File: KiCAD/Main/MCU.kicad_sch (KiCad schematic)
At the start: 8 parts, among them U1 STM32H730VBTx

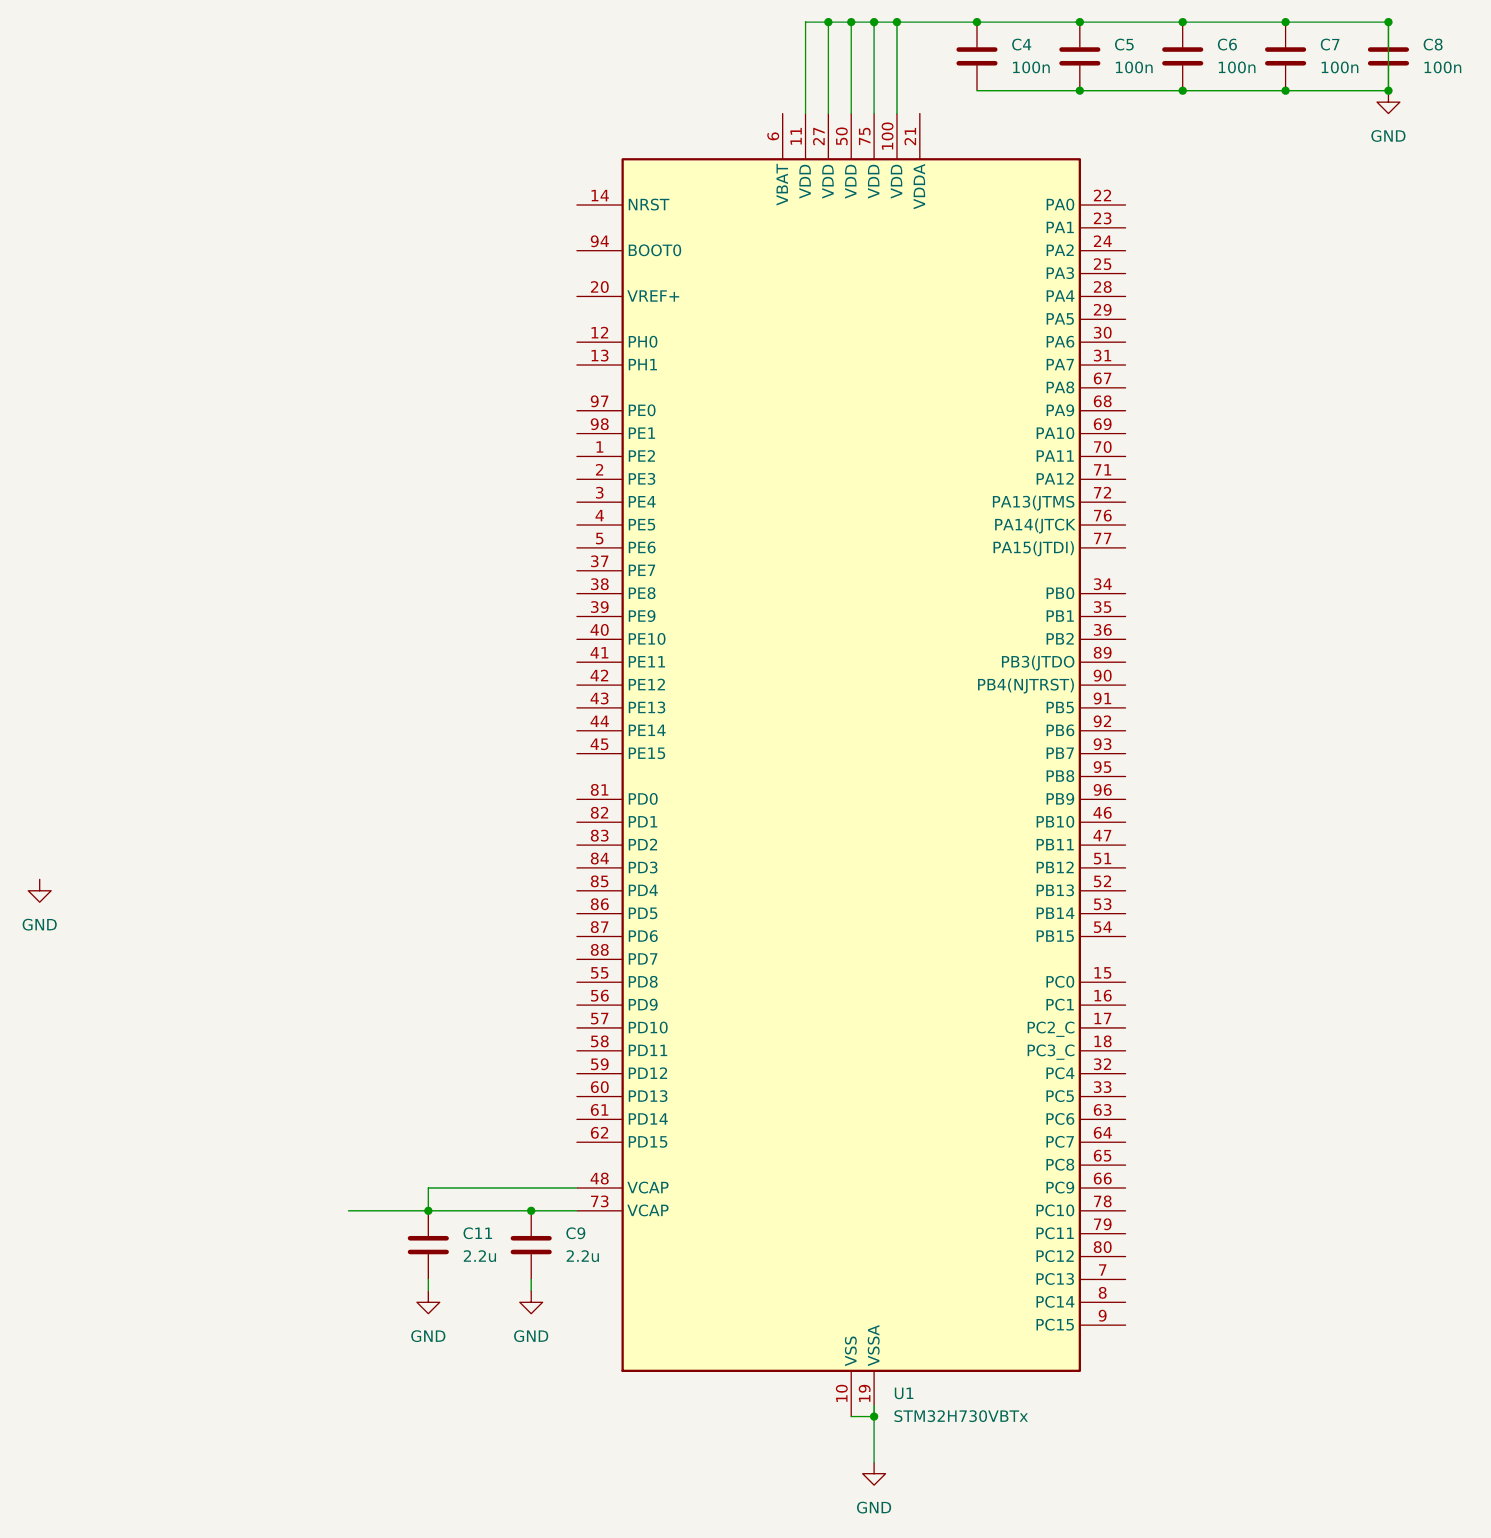
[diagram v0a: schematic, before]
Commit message: Update MCU to display connections
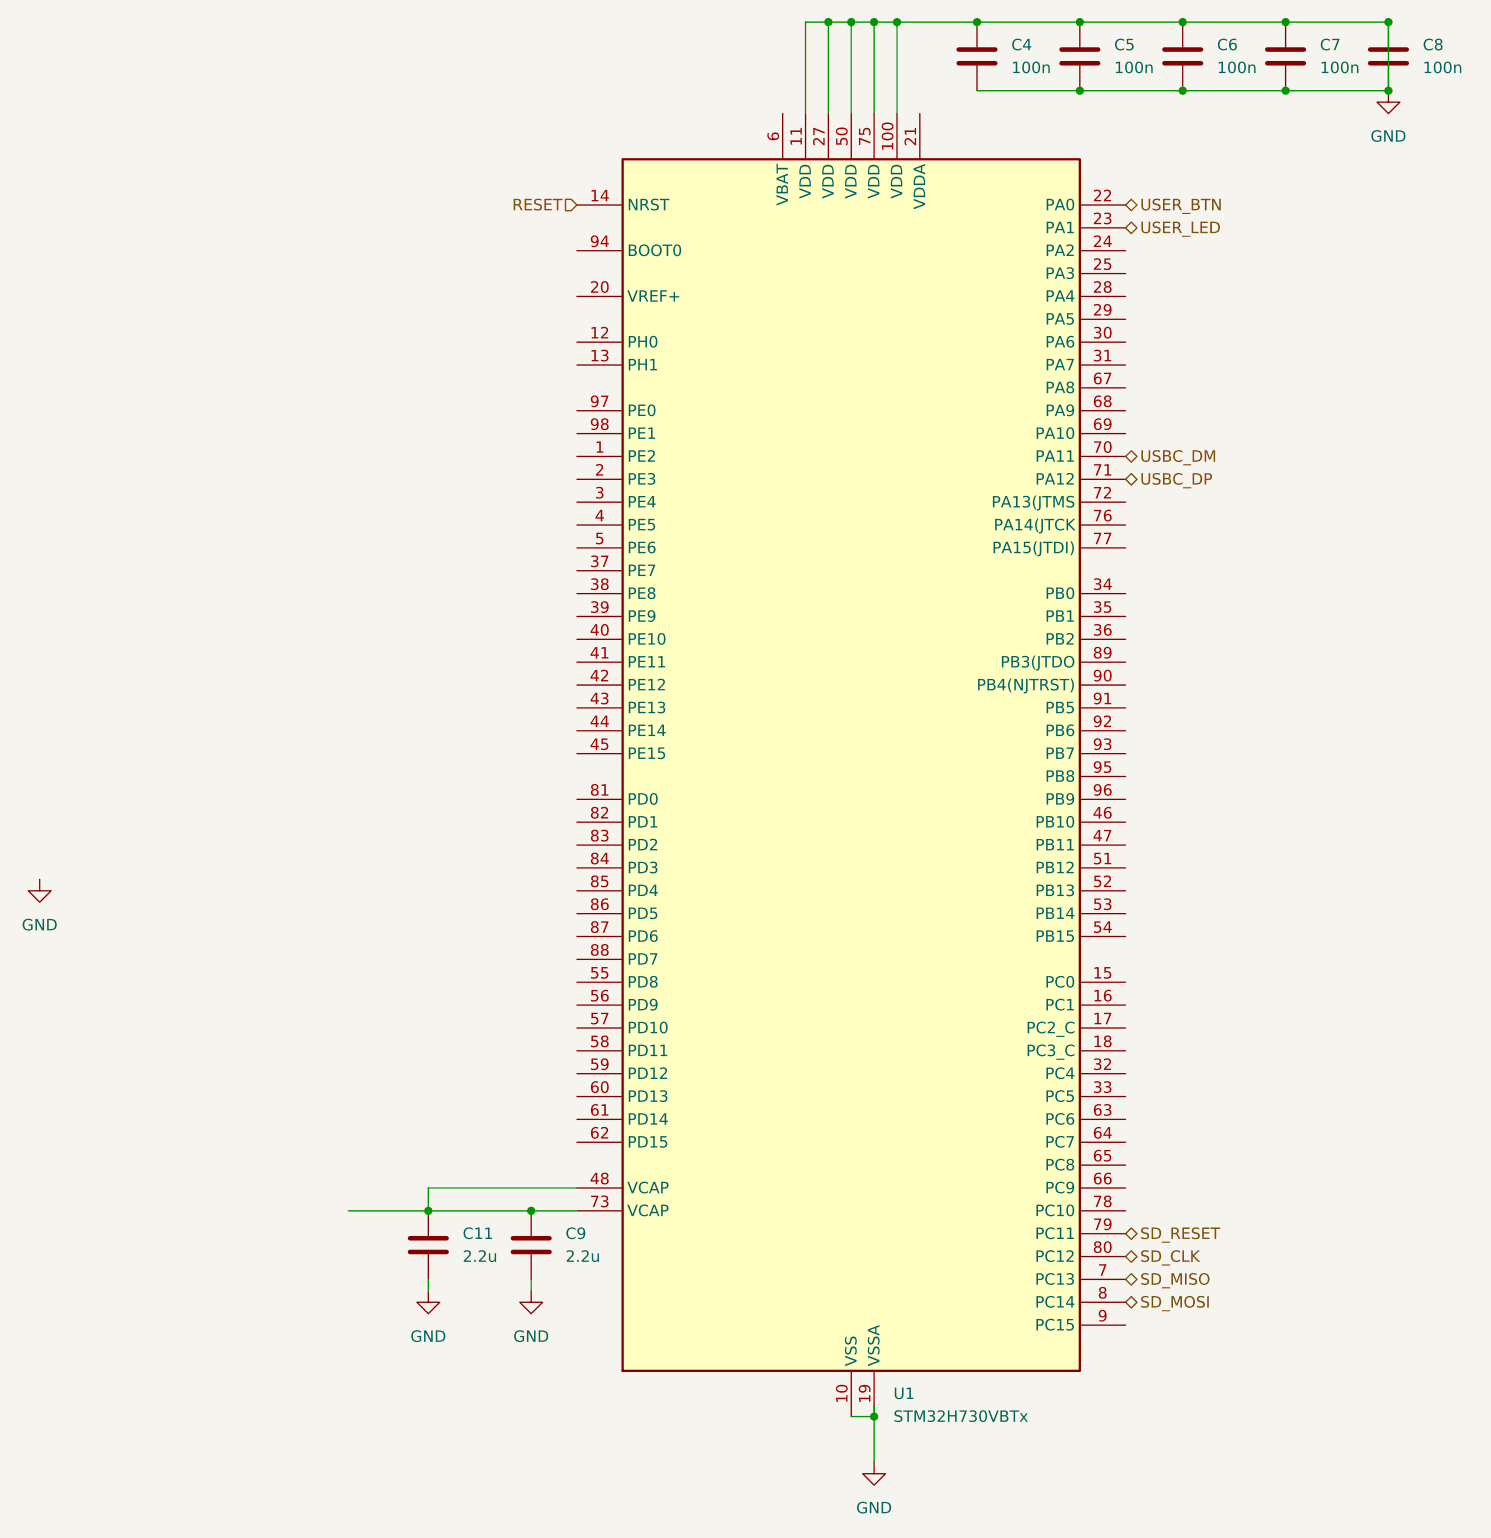
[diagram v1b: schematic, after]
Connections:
- net RESET: now reaches U1.14 (NRST)
- net USER_BTN: now reaches U1.22 (PA0)
- net USER_LED: now reaches U1.23 (PA1)
- net SD_MISO: now reaches U1.7 (PC13)
- net USBC_DM: now reaches U1.70 (PA11)
- net USBC_DP: now reaches U1.71 (PA12)
- net SD_RESET: now reaches U1.79 (PC11)
- net SD_MOSI: now reaches U1.8 (PC14)
- net SD_CLK: now reaches U1.80 (PC12)

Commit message: Fix labeling issue
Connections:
- net GPS_RESET: now reaches U1.24 (PA2)
- net USER LED: now reaches U1.33 (PC5)
- net USER BTN: now reaches U1.34 (PB0)
- net USER_BTN renamed GPS_RX
- net USER_LED renamed GPS_TX

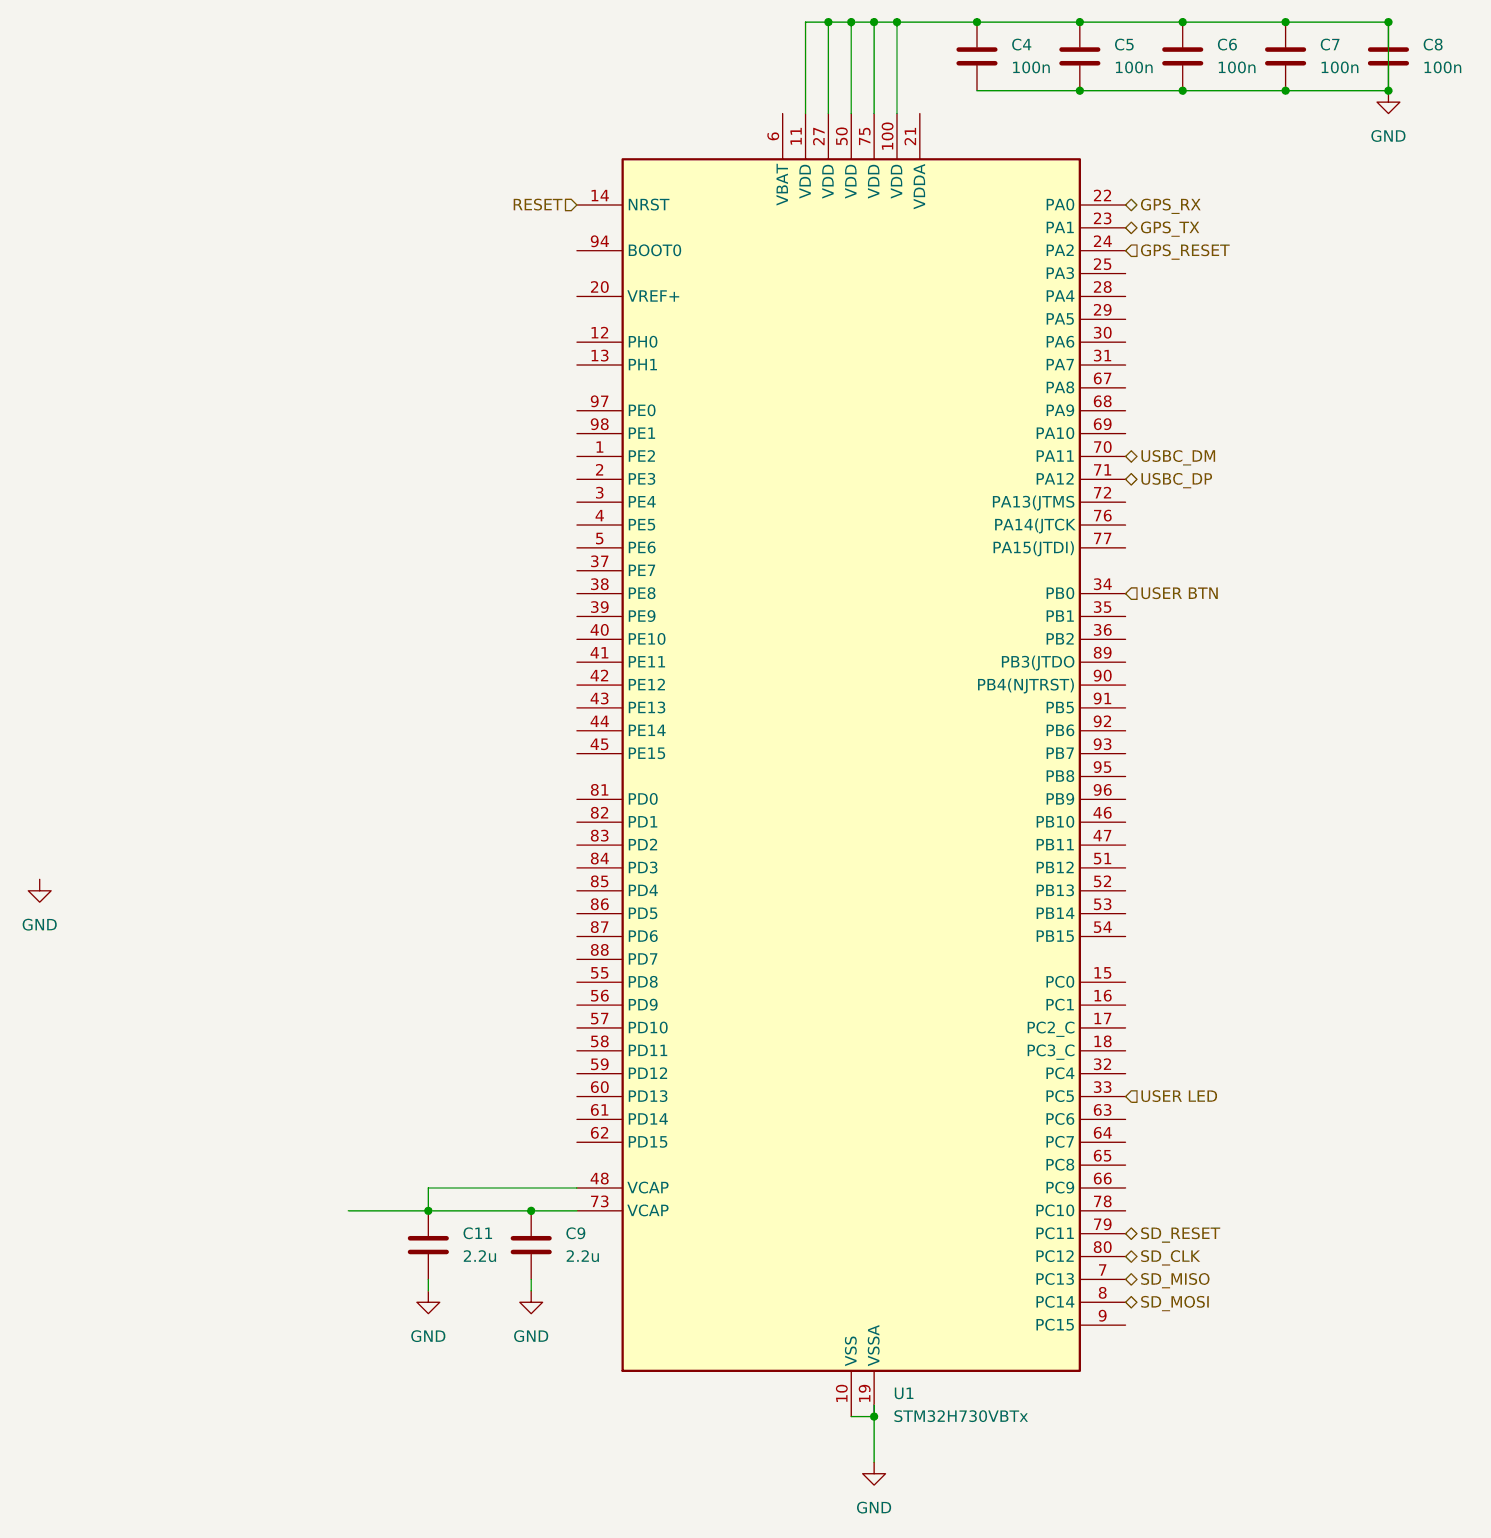
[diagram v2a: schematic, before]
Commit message: Add pin assignments for other sensors
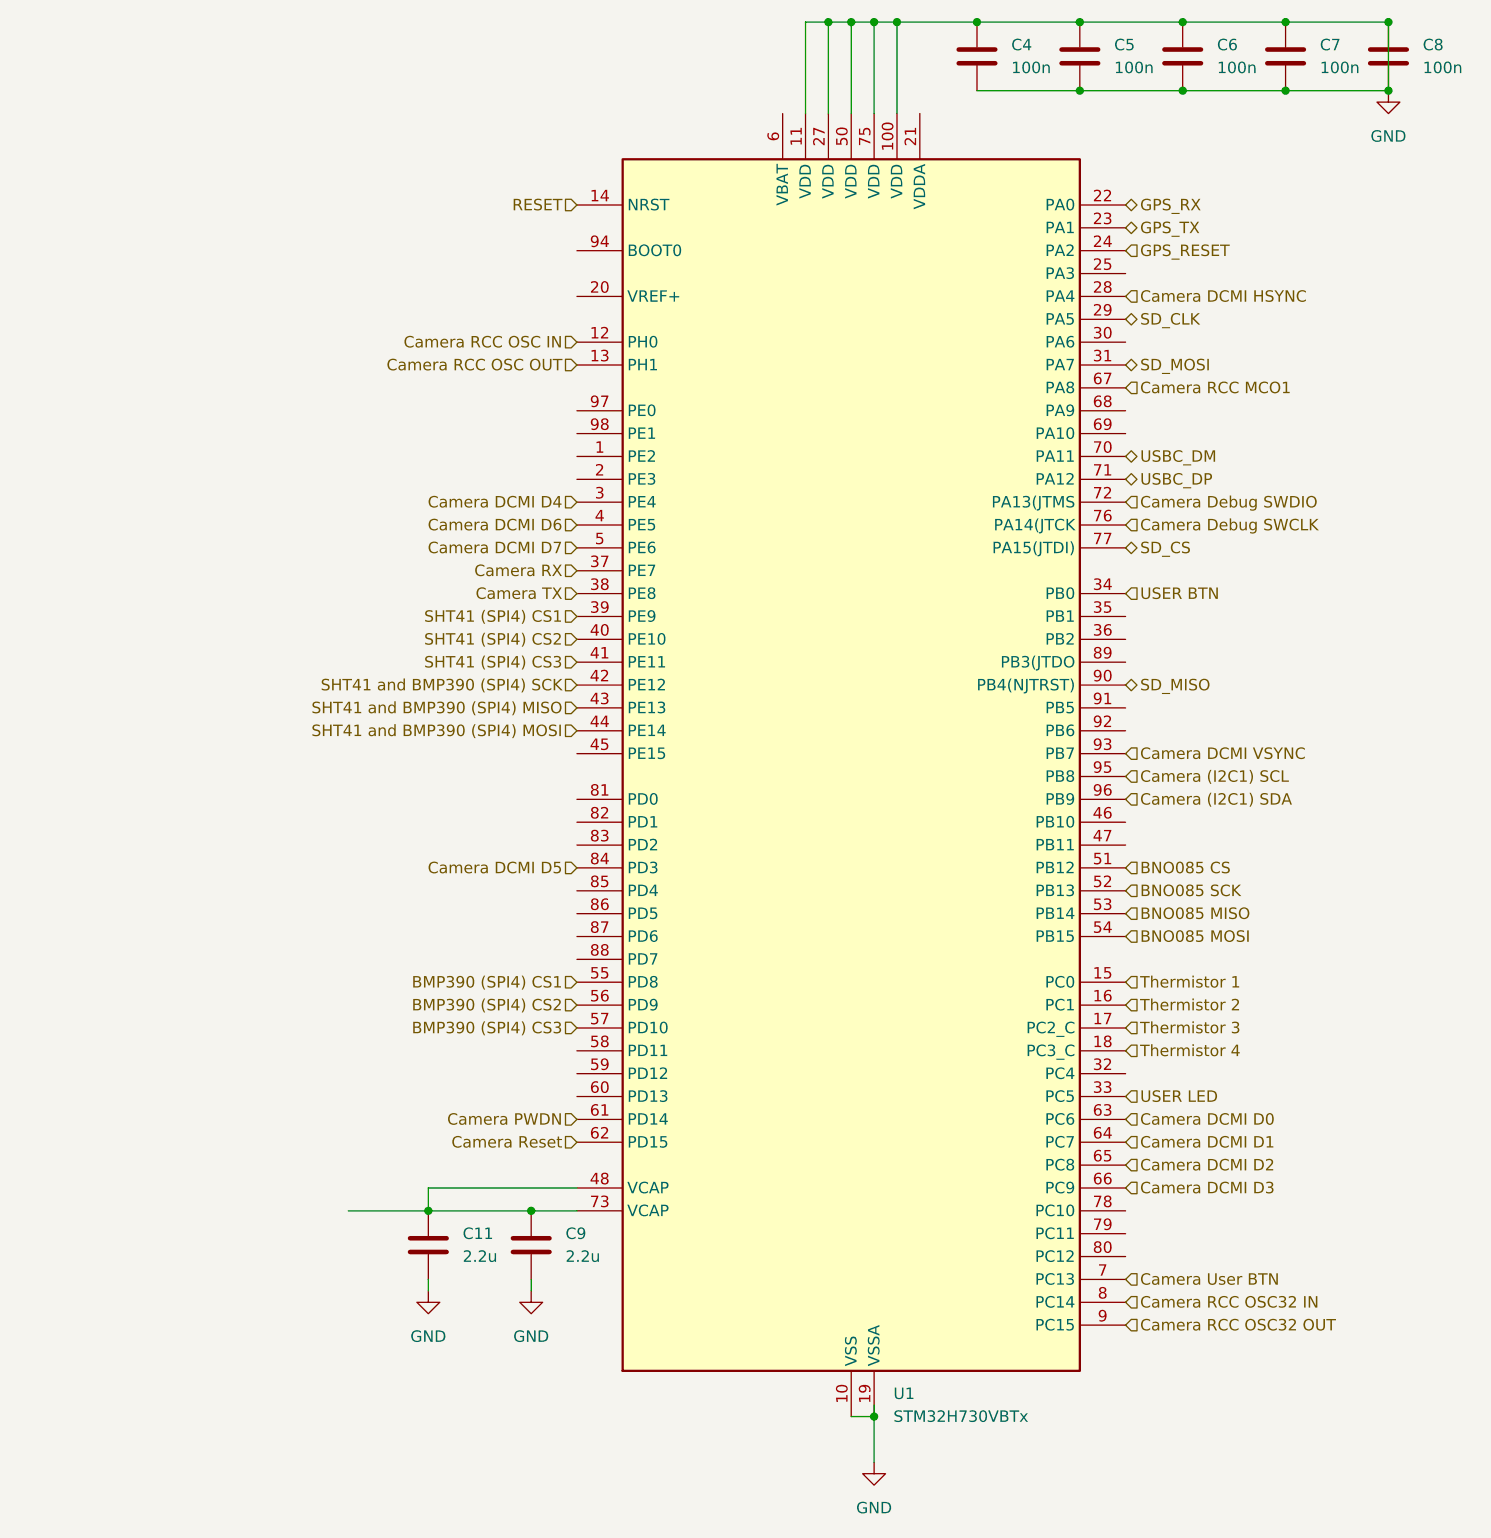
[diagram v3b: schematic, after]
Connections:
- net SD_CLK: now also U1.29 (PA5); no longer U1.80 (PC12)
- net SD_MISO: now also U1.90 (PB4(NJTRST)); no longer U1.7 (PC13)
- net SD_MOSI: now also U1.31 (PA7); no longer U1.8 (PC14)
- net Camera RCC OSC IN: now reaches U1.12 (PH0)
- net Camera RCC OSC OUT: now reaches U1.13 (PH1)
- net Thermistor 1: now reaches U1.15 (PC0)
- net Thermistor 2: now reaches U1.16 (PC1)
- net Thermistor 3: now reaches U1.17 (PC2_C)
- net Thermistor 4: now reaches U1.18 (PC3_C)
- net Camera DCMI HSYNC: now reaches U1.28 (PA4)
- net Camera DCMI D4: now reaches U1.3 (PE4)
- net Camera RX: now reaches U1.37 (PE7)
- net Camera TX: now reaches U1.38 (PE8)
- net SHT41 (SPI4) CS1: now reaches U1.39 (PE9)
- net Camera DCMI D6: now reaches U1.4 (PE5)
- net SHT41 (SPI4) CS2: now reaches U1.40 (PE10)
- net SHT41 (SPI4) CS3: now reaches U1.41 (PE11)
- net SHT41 and BMP390 (SPI4) SCK: now reaches U1.42 (PE12)
- net SHT41 and BMP390 (SPI4) MISO: now reaches U1.43 (PE13)
- net SHT41 and BMP390 (SPI4) MOSI: now reaches U1.44 (PE14)
- net Camera DCMI D7: now reaches U1.5 (PE6)
- net BNO085 CS: now reaches U1.51 (PB12)
- net BNO085 SCK: now reaches U1.52 (PB13)
- net BNO085 MISO: now reaches U1.53 (PB14)
- net BNO085 MOSI: now reaches U1.54 (PB15)
- net BMP390 (SPI4) CS1: now reaches U1.55 (PD8)
- net BMP390 (SPI4) CS2: now reaches U1.56 (PD9)
- net BMP390 (SPI4) CS3: now reaches U1.57 (PD10)
- net Camera PWDN: now reaches U1.61 (PD14)
- net Camera Reset: now reaches U1.62 (PD15)
- net Camera DCMI D0: now reaches U1.63 (PC6)
- net Camera DCMI D1: now reaches U1.64 (PC7)
- net Camera DCMI D2: now reaches U1.65 (PC8)
- net Camera DCMI D3: now reaches U1.66 (PC9)
- net Camera RCC MCO1: now reaches U1.67 (PA8)
- net Camera Debug SWDIO: now reaches U1.72 (PA13(JTMS)
- net Camera Debug SWCLK: now reaches U1.76 (PA14(JTCK)
- net SD_CS: now reaches U1.77 (PA15(JTDI))
- net Camera DCMI D5: now reaches U1.84 (PD3)
- net Camera RCC OSC32 OUT: now reaches U1.9 (PC15)
- net Camera DCMI VSYNC: now reaches U1.93 (PB7)
- net Camera (I2C1) SCL: now reaches U1.95 (PB8)
- net Camera (I2C1) SDA: now reaches U1.96 (PB9)
- net SD_RESET: no longer names the net of U1.79 (PC11)
- new net Camera RCC OSC32 IN: U1.8 (PC14)
- new net Camera User BTN: U1.7 (PC13)
